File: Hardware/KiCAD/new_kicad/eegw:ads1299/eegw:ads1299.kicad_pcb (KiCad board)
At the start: 2 copper layers, 108.1 x 114.1 mm, 48 parts, among them J1 ESP32_R2, J11 ESP32_L, J2 gpioADS, J3 ESP32_Left, J4 L, J5 ESP32_Right, J6 R, J7 ESP32_R1, J9 ESP32_R3, U1 ADS1299IPAG

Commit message: update filled zone & geograpgically annotated pcb
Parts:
- J7: renamed from J4; value L -> N
- J8: renamed from J6; value R -> P
- renumbered C4 to C1, C28 to C10, C12 to C11, C19 to C12, C3 to C13, C20 to C14, C9 to C15, C13 to C16, C10 to C17, C17 to C2, C16 to C3, C1 to C4, C7 to C6, C6 to C7, C18 to C8, C2 to C9, J3 to J1, J11 to J2, J7 to J3, J5 to J4, J9 to J5, J1 to J6, J2 to J9, JP4 to JP1, JP3 to JP2, JP2 to JP3, JP1 to JP4, R7 to R1, R13 to R10, R19 to R11, R11 to R2, R17 to R3, R14 to R4, R9 to R5, R10 to R6, R8 to R7, R18 to R8, R21 to R9, U2 to U1, U4 to U2, U6 to U3, U5 to U4, U3 to U5, U1 to U6, U8 to U7
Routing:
- added copper zone on B.Cu, net (none)
- added copper zone on F.Cu, net (none)

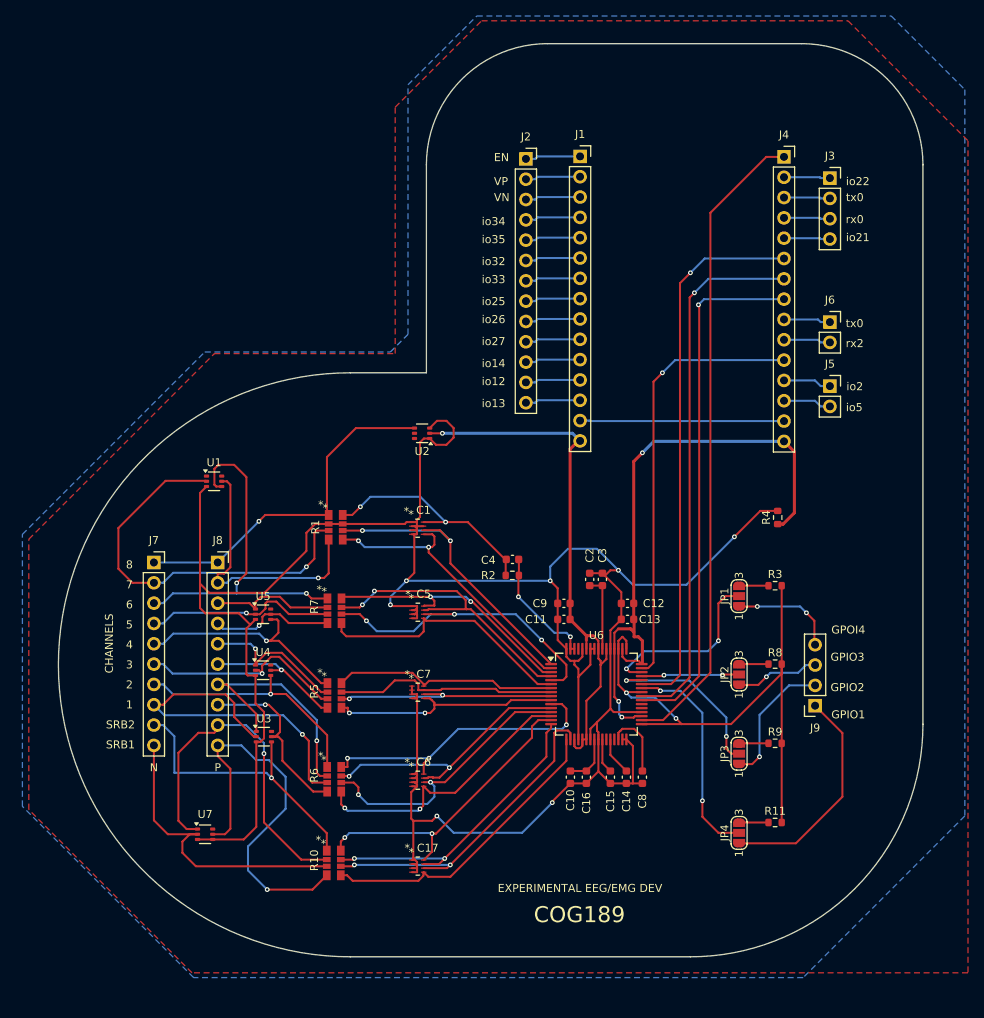
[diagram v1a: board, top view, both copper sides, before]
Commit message: fixed zone fills for GNDA/GNDD/GND &added grb file
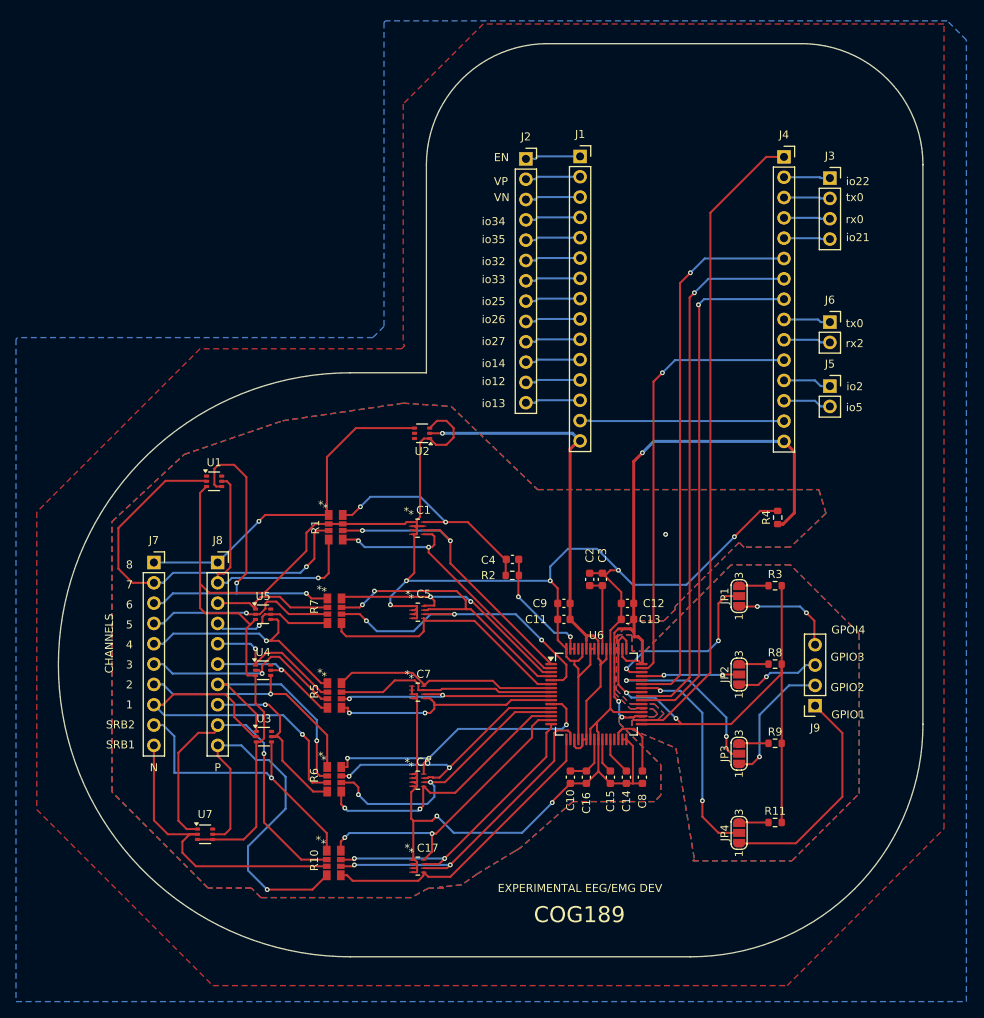
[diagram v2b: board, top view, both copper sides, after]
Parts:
- C4: value 1.5n -> 1n
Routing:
- net GND: vias 0 -> 1
- added copper zone on B.Cu, net GND
- added copper zone on B.Cu, net GNDA
- added copper zone on F.Cu, net GNDA
- added copper zone on B.Cu, net GNDD
- added copper zone on F.Cu, net GNDD
- removed copper zone on B.Cu, net (none)
